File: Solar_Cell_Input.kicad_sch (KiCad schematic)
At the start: 30 parts, among them Q201 NMOS, Q202 NMOS, Q203 NMOS, Q303 NMOS, U201 BQ24650, U301 TMCS1101A2UQDT

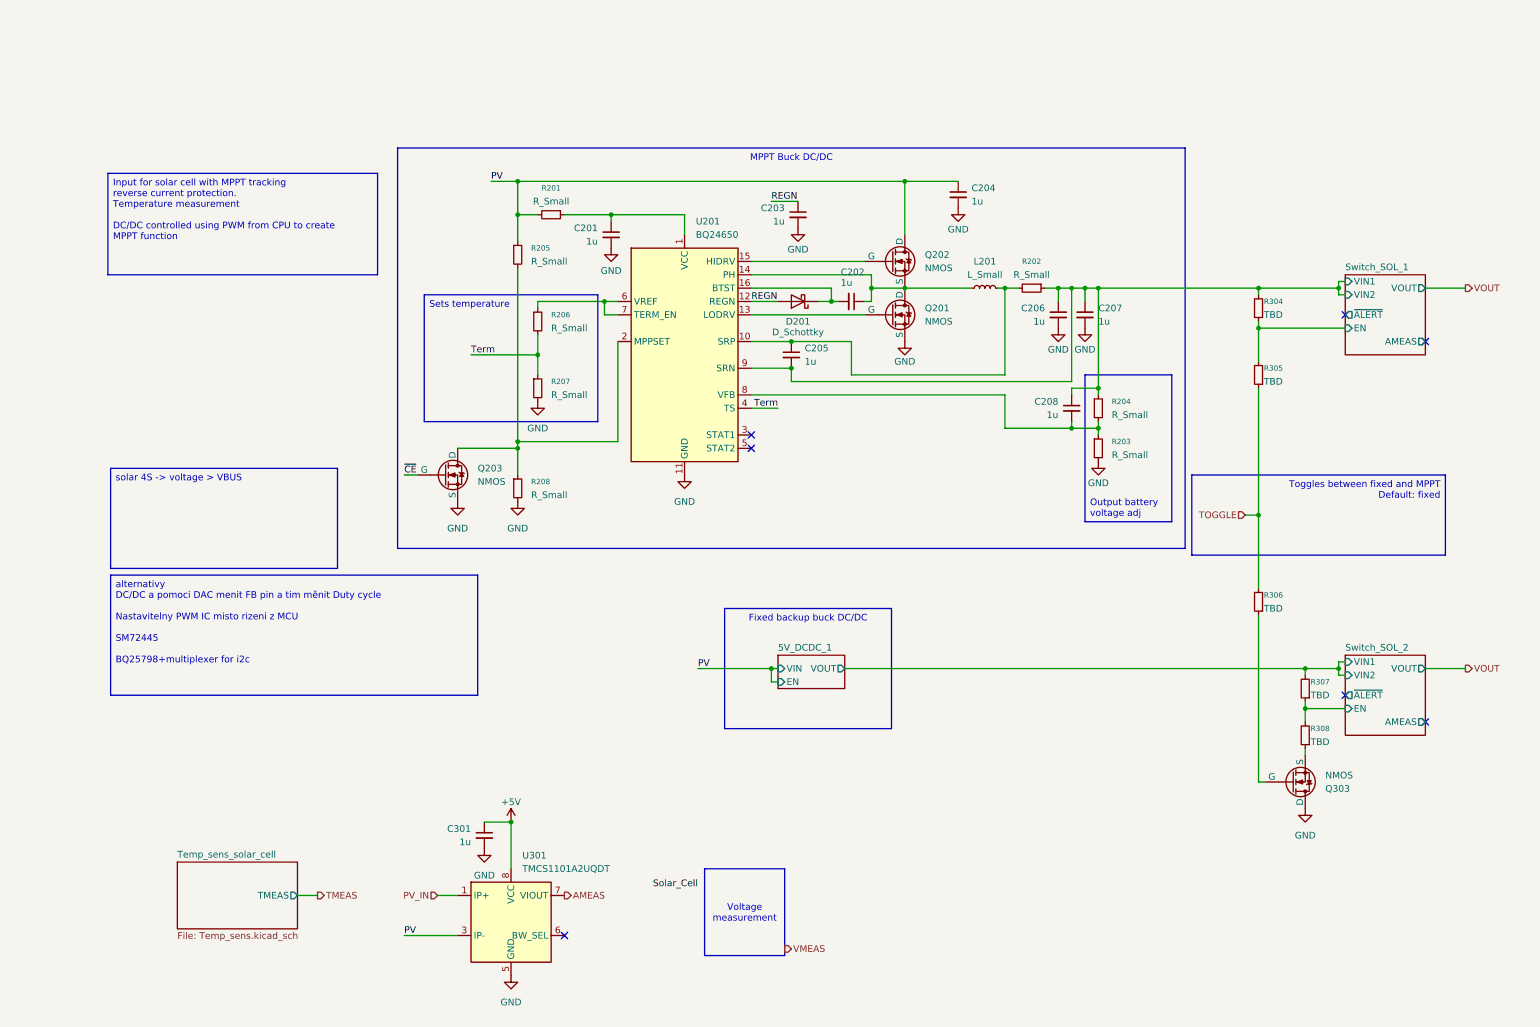
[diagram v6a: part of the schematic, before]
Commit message: updated battery pack module; updated solar inputs module
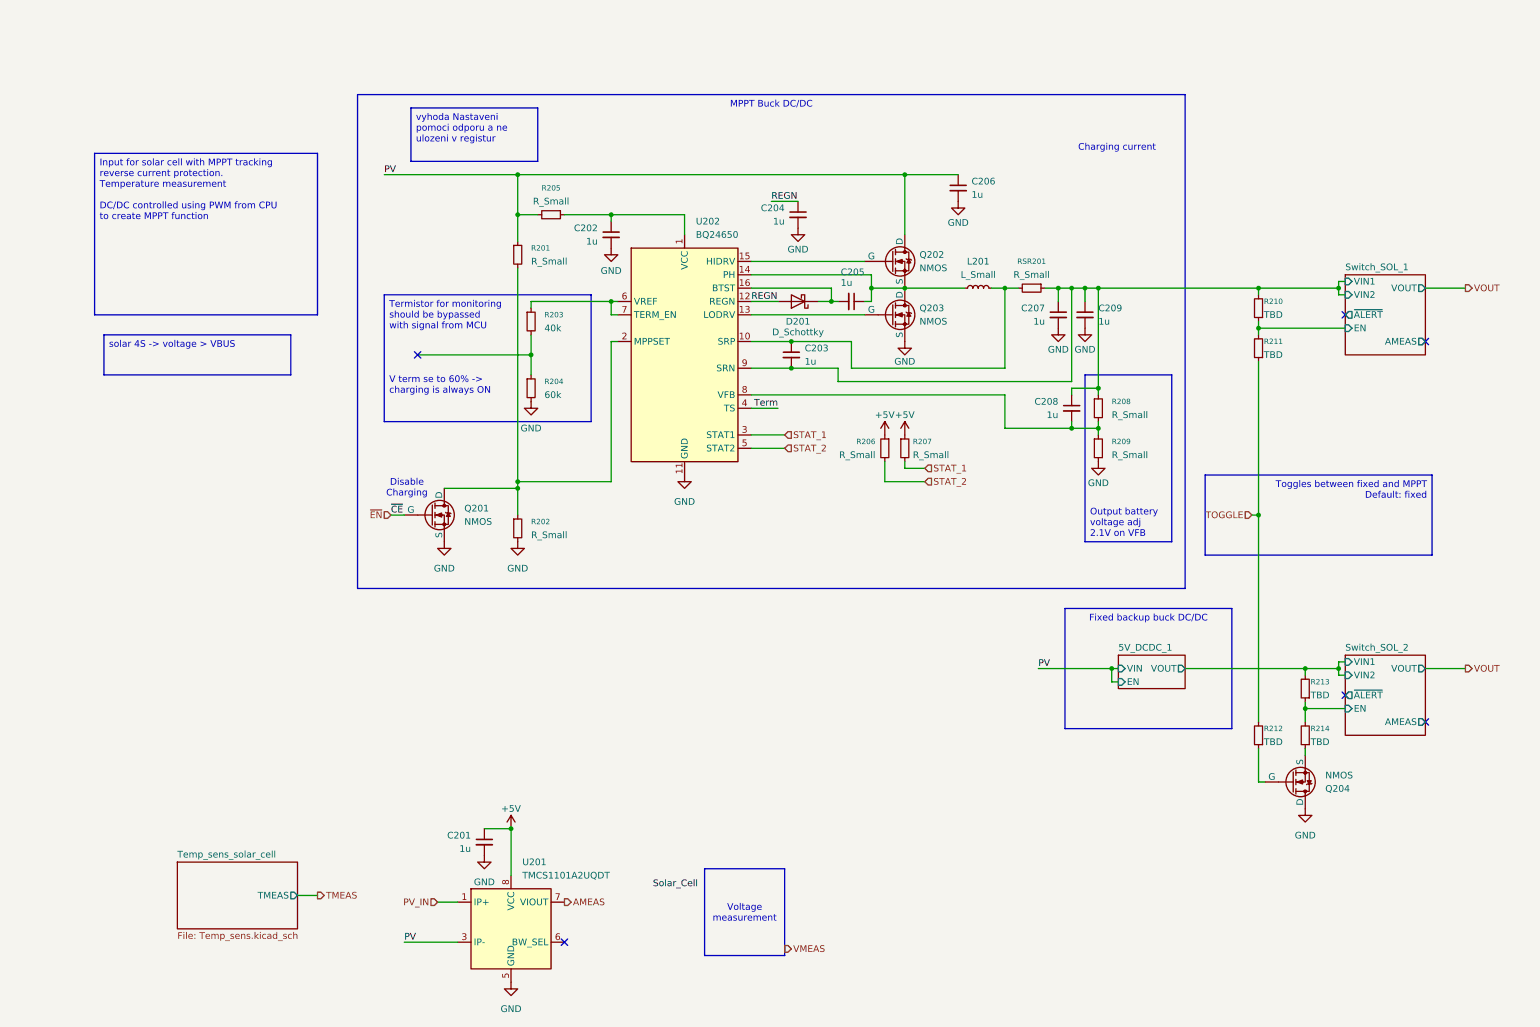
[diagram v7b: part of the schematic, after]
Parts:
- added R206, R207: R_Small, Resistor_SMD:R_0603_1608Metric_Pad0.98x0.95mm_HandSolder, symbol Device:R_Small
- R203: renamed from R206; value R_Small -> 40k
- R204: renamed from R207; value R_Small -> 60k
- renumbered C301 to C201, C201 to C202, C205 to C203, C203 to C204, C202 to C205, C204 to C206, C206 to C207, C207 to C209, Q203 to Q201, Q201 to Q203, Q303 to Q204, R205 to R201, R208 to R202, R201 to R205, R204 to R208, R203 to R209, R304 to R210, R305 to R211, R306 to R212, R307 to R213, R308 to R214, R202 to RSR201, U301 to U201, U201 to U202
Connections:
- net +5V: now also R206.1, R207.1
- net Term: no longer R203.2, R204.1
- net STAT_1: now reaches U202.3 (STAT1)
- net STAT_1: now also R207.2
- net STAT_2: now reaches U202.5 (STAT2)
- net STAT_2: now also R206.2
- net ~{CE} renamed ~{EN}
- new net: R203.2, R204.1
- no-connect marks 7 -> 6
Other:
- note added: "Charging current"
- note added: "Disable Charging"
- moved on the sheet: C201, C206, L201, Q201, R202, R203, R204, R211, R212, U201

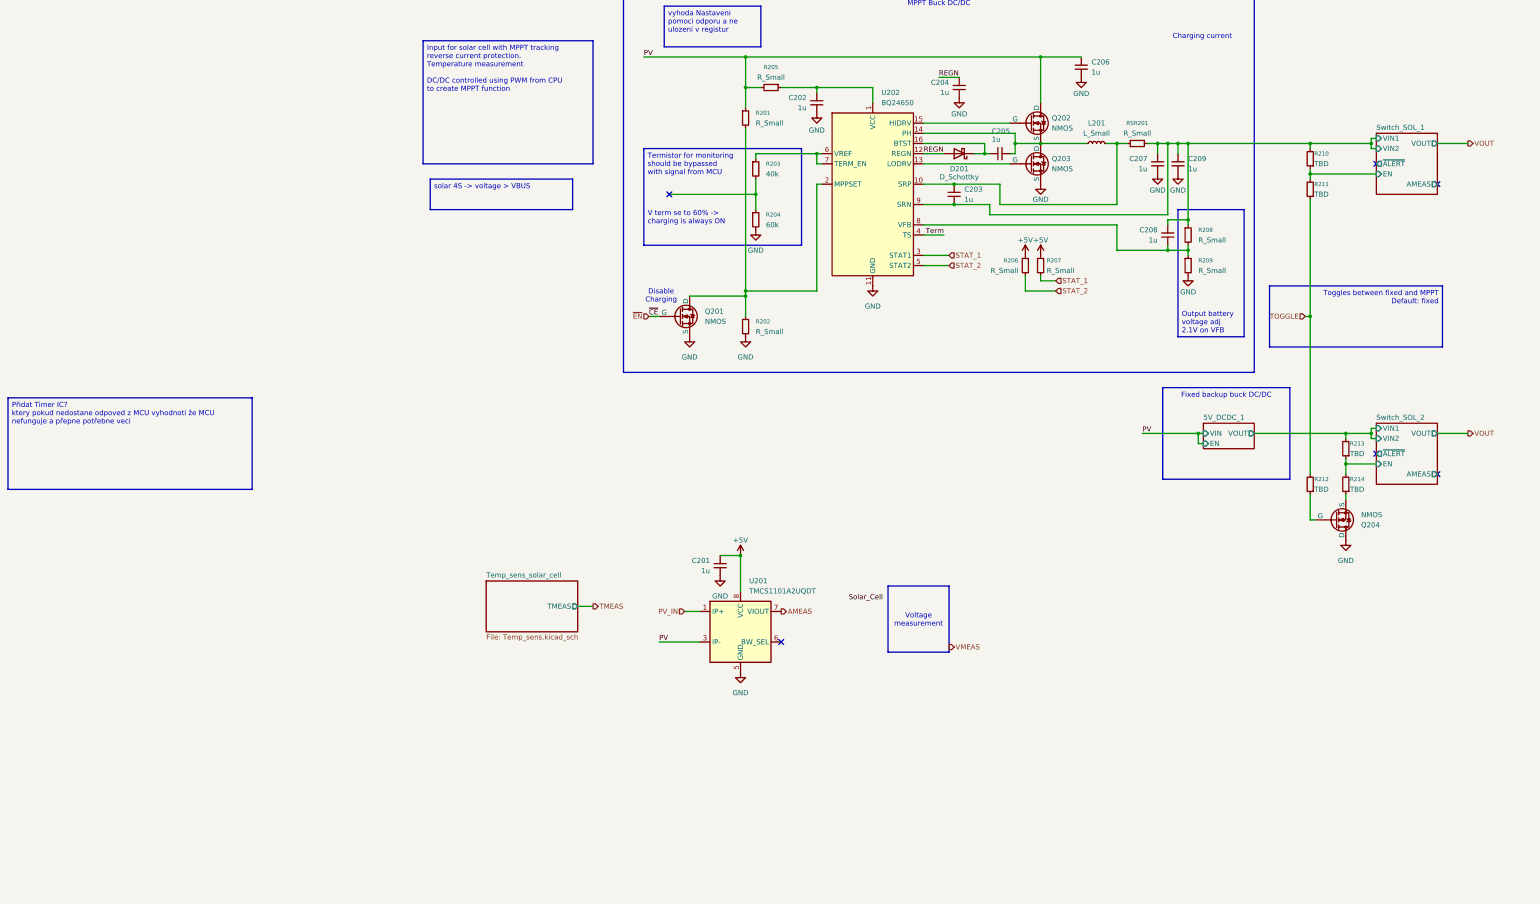
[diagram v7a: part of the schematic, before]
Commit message: added values to most parts
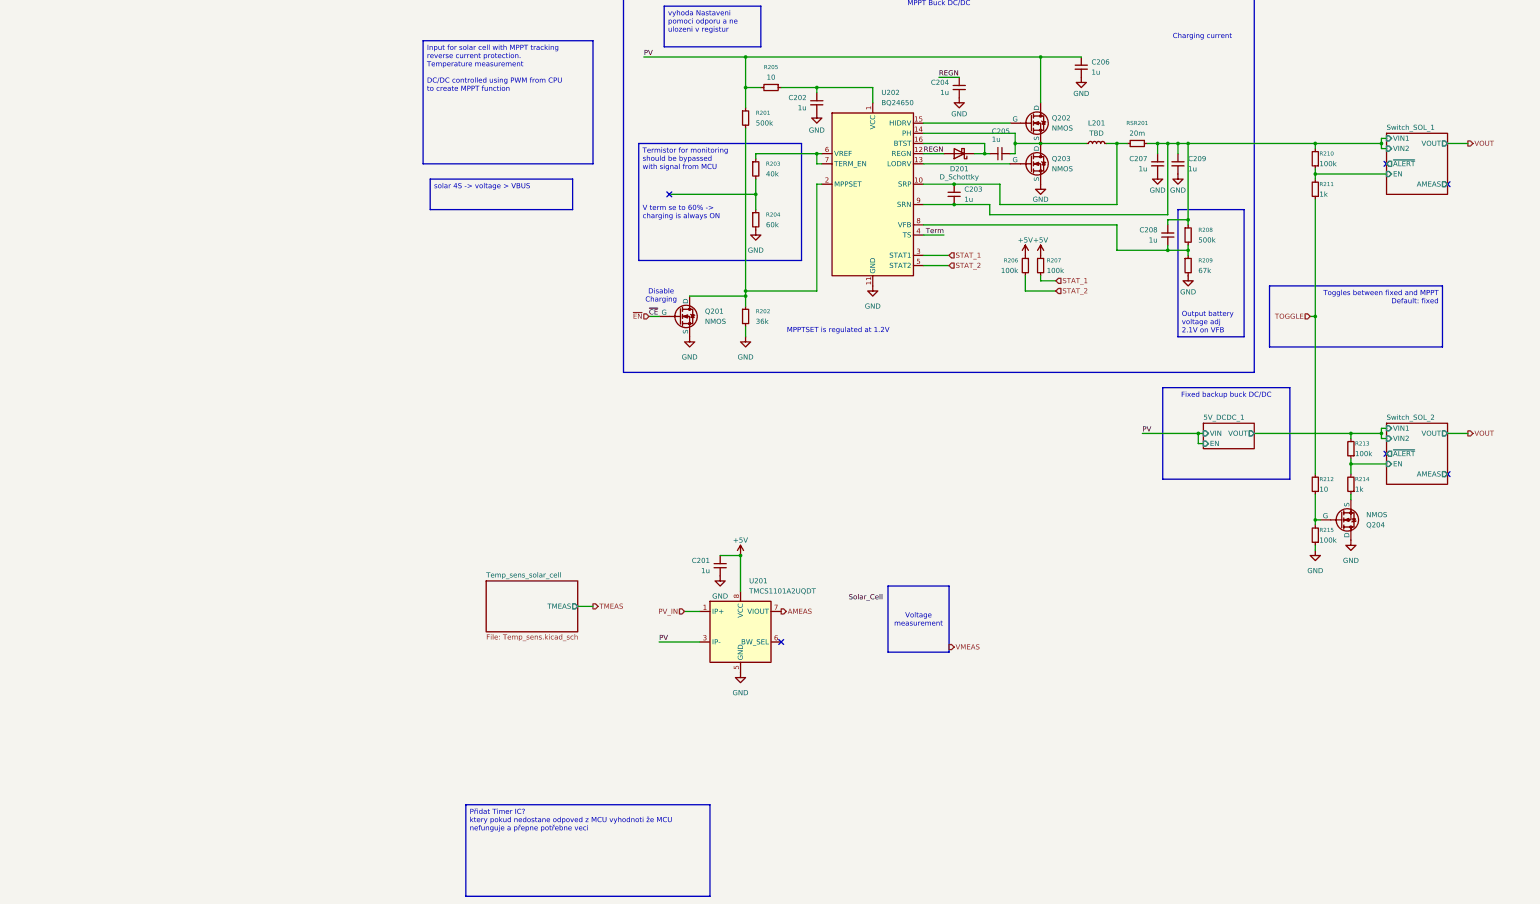
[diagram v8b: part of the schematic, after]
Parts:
- added R215: 100k, Resistor_SMD:R_0603_1608Metric_Pad0.98x0.95mm_HandSolder, symbol Device:R_Small
- L201: value L_Small -> TBD
- R201, R208: value R_Small -> 500k
- R202: value R_Small -> 36k
- R205: value R_Small -> 10
- R206, R207: value R_Small -> 100k
- R209: value R_Small -> 67k
- R210, R213: value TBD -> 100k
- R211, R214: value TBD -> 1k
- R212: value TBD -> 10
- RSR201: value R_Small -> 20m
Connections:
- net GND: now also R215.1
- net at Q204.2 (G), R212.1: now also R215.2
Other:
- note added: "MPPTSET is regulated at 1.2V"
- moved on the sheet: Q204, R202, R210, R211, R212, R213, R214
